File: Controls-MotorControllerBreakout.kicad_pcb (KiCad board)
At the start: 2 copper layers, 47.8 x 44.5 mm, 54 parts, among them J1 MC CAN 1, J2 MC CAN 2, J3 CTRLS, J4 EXT PWR, J5 CANDAPTER, Q1 PMV35EPER, Q2 PMV35EPER, Q3 RUM001L02T2CL, Q4 RE1C001ZPTL, U1 TPS2121RUXR

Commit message: remove silkscreen comment
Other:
- board text removed: "check all silks"
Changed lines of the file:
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@@
 		)
 		(property "Value" "375mA"
-			(at 0 1.82 360)
+			(at 0 1.82 0)
 			(layer "F.Fab")
 			(effects
@@
 		)
 		(fp_text user "${REFERENCE}"
-			(at 0 0 360)
+			(at 0 0 0)
 			(layer "F.Fab")
 			(effects
@@
 	)
 	(gr_rect
-		(start 119.5 71.75)
-		(end 106 76.5)
+		(start 106 71.75)
+		(end 119.5 76.5)
 		(stroke
 			(width 0.1)
@@
 		)
 	)
-	(gr_text "check all silks"
-		(at 59.75 30.5 0)
-		(layer "Cmts.User")
-		(effects
-			(font
-				(size 1 1)
-				(thickness 0.15)
-			)
-			(justify left bottom)
-		)
-	)
 	(dimension
 		(type orthogonal)
@@
 				(xy 98 67.25) (xy 96.25 67.25) (xy 94.25 67.25) (xy 93.75 66.75) (xy 87.5 66.75) (xy 87.25 47.5)
 				(xy 93 47.5) (xy 93 50) (xy 91 50) (xy 90.5 50.5) (xy 90.5 57.75) (xy 90.5 60.25) (xy 90.75 60.5)
-				(xy 90.75 62) (xy 90.5 62.25) (xy 90.5 64.25) (xy 91 64.75) (xy 98 64.75) (xy 98 65.25) (xy 98 65.25)
-				(xy 98 65.25) (xy 98 67.25)
+				(xy 90.75 62) (xy 90.5 62.25) (xy 90.5 64.25) (xy 91 64.75) (xy 98 64.75) (xy 98 65.25)
 			)
 		)
@@
 		(polygon
 			(pts
-				(xy 93.9 72.5125) (xy 92.1 72.5125) (xy 92.1 72.5125) (xy 90.2 72.5125) (xy 90.2 70.5125) (xy 93.9 70.5125)
+				(xy 93.9 72.5125) (xy 92.1 72.5125) (xy 90.2 72.5125) (xy 90.2 70.5125) (xy 93.9 70.5125)
 			)
 		)

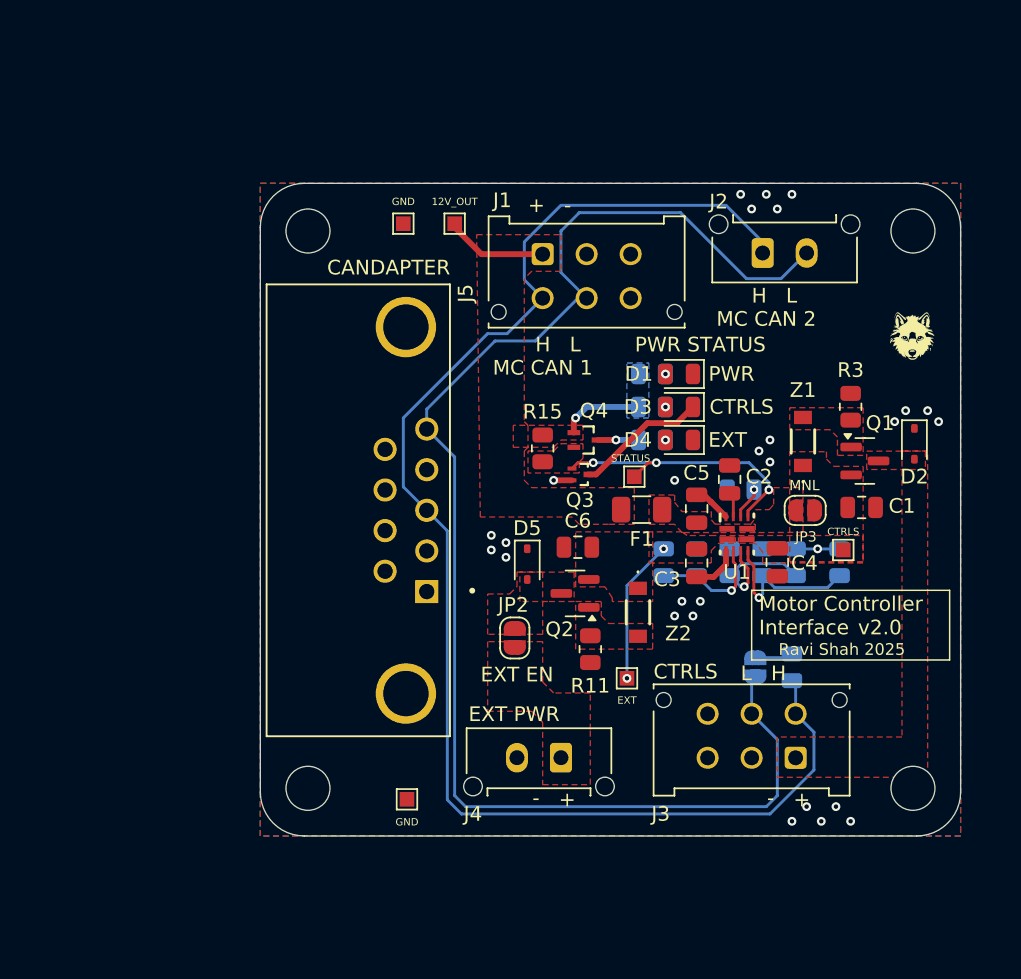
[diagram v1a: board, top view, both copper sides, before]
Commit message: add fan conns, layout + routing
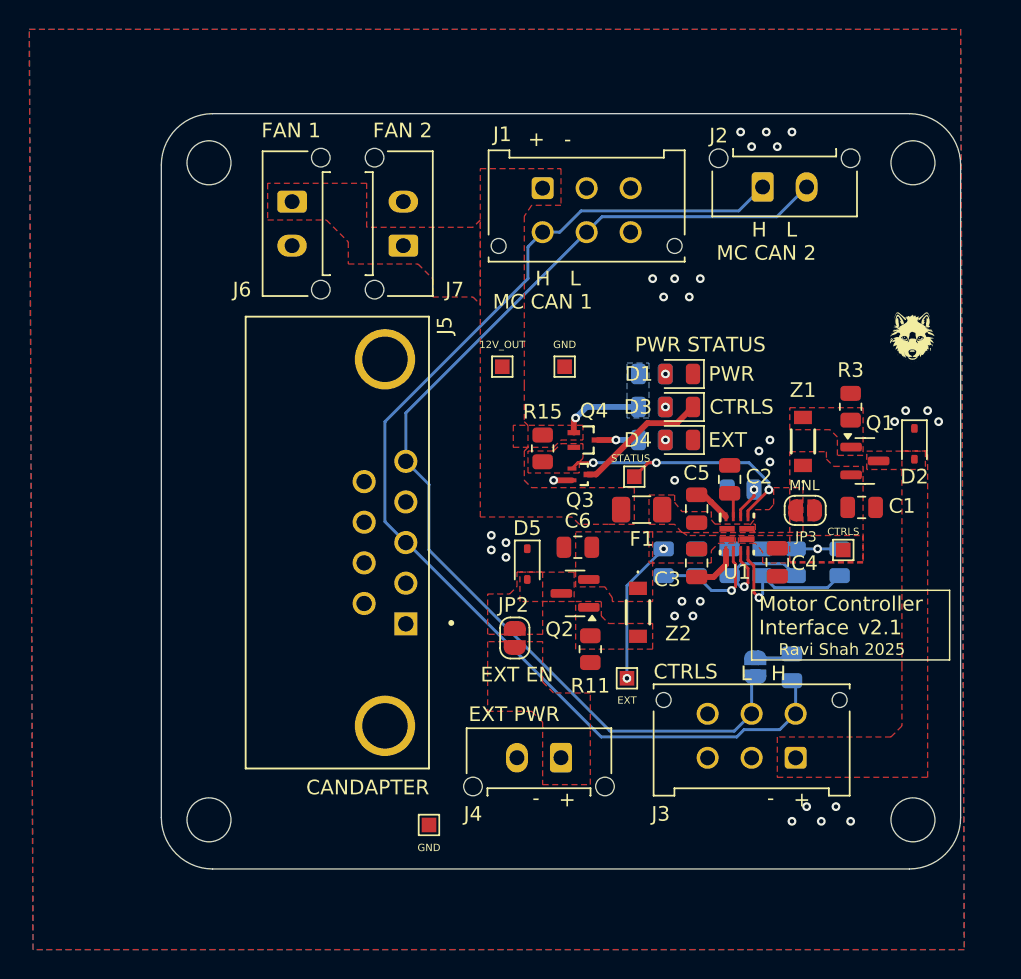
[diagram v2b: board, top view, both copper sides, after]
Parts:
- added J6: FAN 1, Connector_Molex:Molex_Micro-Fit_3.0_43650-0215_1x02_P3.00mm_Vertical, F.Cu at (74.7, 45.2)
- added J7: FAN 2, Connector_Molex:Molex_Micro-Fit_3.0_43650-0215_1x02_P3.00mm_Vertical, F.Cu at (82.2, 48.2)
- F1: value 375mA -> 2A
- R4: value 100k -> 44.2k (TBD)
- moved LOGO1 37.3 mm to (147.0, 66.5)
- moved TP3 14.7 mm to (93.2, 56.5)
- moved TP4 10.3 mm to (89.0, 56.5)
- moved H1 8.20 mm to (69.0, 42.6)
- moved H2 7.08 mm to (69.0, 87.4)
- moved H4 4.65 mm to (117.0, 42.6)
- moved J1 4.50 mm to (91.8, 44.3)
- moved J2 4.50 mm to (106.8, 44.2)
- moved J5 2.62 mm to (81.0, 68.5)
- moved TP6 2.30 mm to (84.0, 87.8)
- moved H3 2.15 mm to (117.0, 87.4)
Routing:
- net /CAN_L: track 97.9 -> 73.9 mm
- net /CAN_H: track 96.9 -> 77.6 mm
- net +12V: track 12.7 -> 5.65 mm
- net GND: vias 27 -> 32
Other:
- board size 47.8 x 44.5 mm -> 54.5 x 51.5 mm
- board text added: "v2.1"
- board text removed: "v2.0"

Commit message: yuhhh
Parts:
- added G***: LOGO, LOGO, B.Cu at (71.5, 65.0)
- moved LOGO1 38.7 mm to (110.2, 54.5)

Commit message: hi its me again
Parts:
- added D6: FLYBK1, UTSVT_Passive:DO-221AC, F.Cu at (70.5, 49.5)
- added D7: FLYBK2, UTSVT_Passive:DO-221AC, F.Cu at (86.0, 46.5)
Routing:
- net GND: vias 32 -> 39
